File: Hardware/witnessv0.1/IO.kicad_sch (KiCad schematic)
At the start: 3 parts, among them J2 Conn_01x02, J3 Conn_01x08, P1 USB_C_Plug_USB2.0

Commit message: power updates and some esp32 stuff
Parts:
- P1: footprint Connector_USB:USB_C_Receptacle_G-Switch_GT-USB-7010ASV -> KicadLibs:CONN_10164359-00011LF_AMP
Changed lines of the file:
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@@
 			)
 		)
-		(property "Footprint" "Connector_USB:USB_C_Receptacle_G-Switch_GT-USB-7010ASV"
+		(property "Footprint" "KicadLibs:CONN_10164359-00011LF_AMP"
 			(at 234.95 113.03 0)
 			(hide yes)

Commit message: lots of work
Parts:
- added R32: 5.1k, Resistor_SMD:R_0603_1608Metric, symbol Device:R_Small
- added U9: USBLC6-2SC6, Package_TO_SOT_SMD:SOT-23-6, symbol Power_Protection:USBLC6-2SC6
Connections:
- net +BATT: now reaches J2.1 (Pin_1)
- net GND: now reaches J2.2 (Pin_2)
- net GND: now also P1.A1 (GND), P1.A12 (GND), P1.B1 (GND), P1.B12 (GND), R32.1, U9.2 (GND)
- net VBUS: now reaches P1.A4 (VBUS), P1.A9 (VBUS), P1.B4 (VBUS), P1.B9 (VBUS)
- net VBUS: now also U9.5 (VBUS)
- net at P1.A5 (CC): now also R32.2
- net at P1.A6 (D+): now also U9.3 (I/O2)
- net at P1.A7 (D-): now also U9.1 (I/O1)
- new net USB_D+: U9.4 (I/O2), U9.6 (I/O1)
- no-connect marks 0 -> 2
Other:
- note added: "INPUTS"
- note added: "OUTPUTS"
- company: (none) -> WITNESS
- title: (none) -> IO
- moved on the sheet: J2, P1

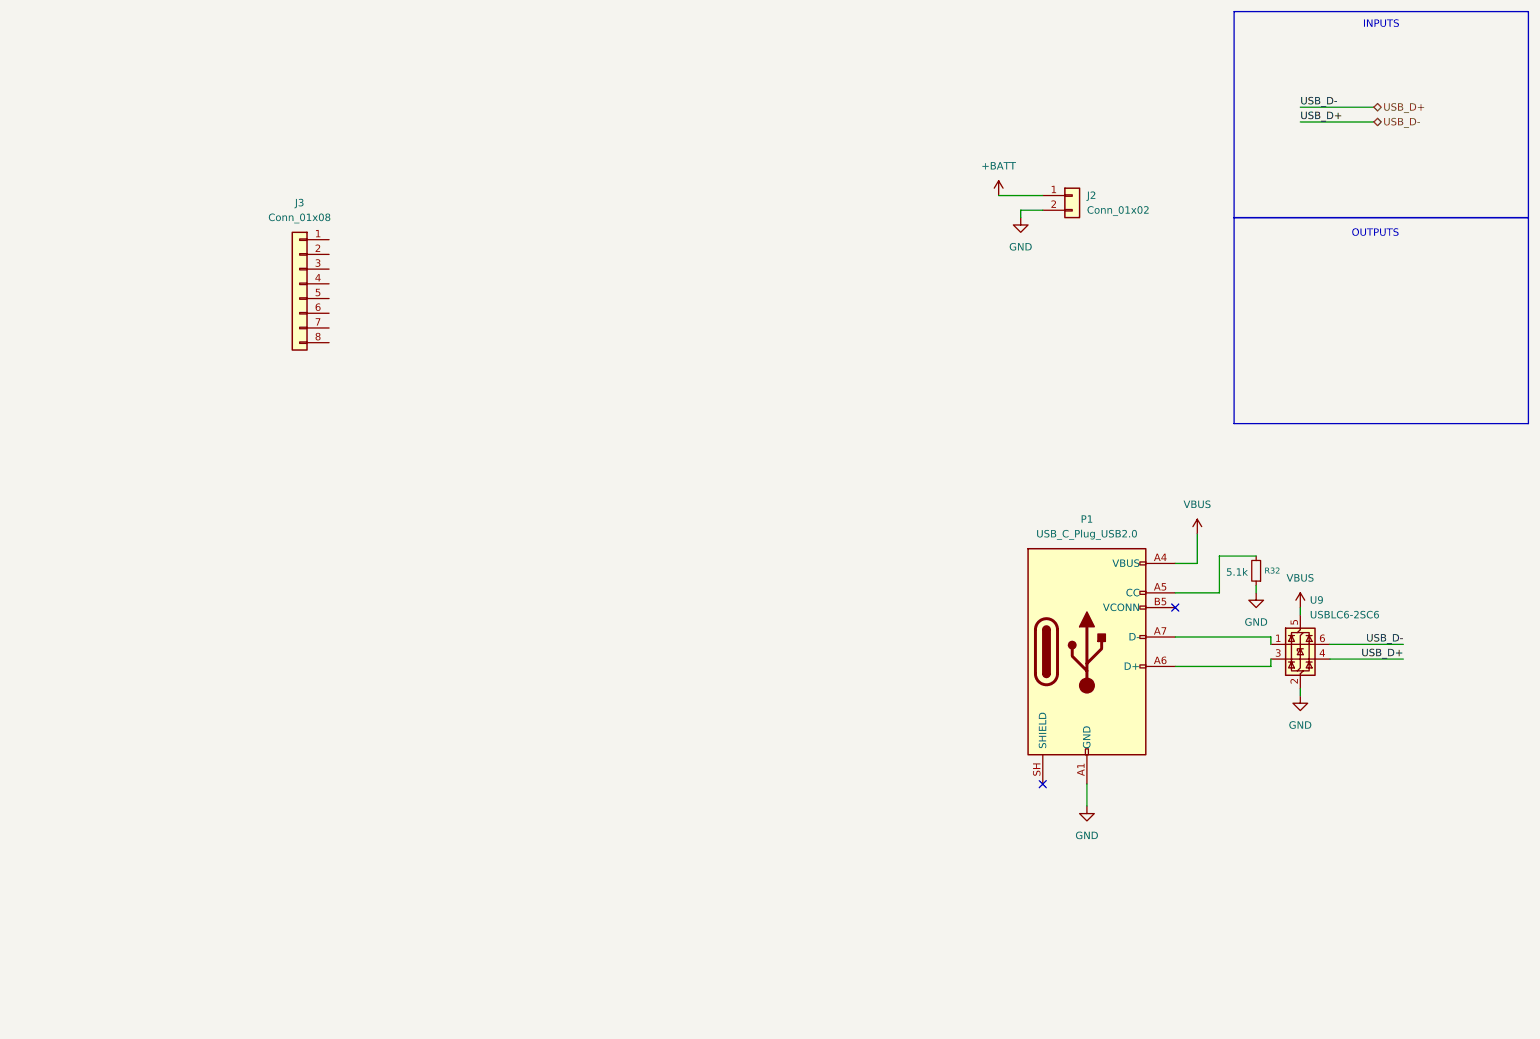
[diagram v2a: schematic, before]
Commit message: micro lock conenctors and sd card soldered to baord and inital palcement done.
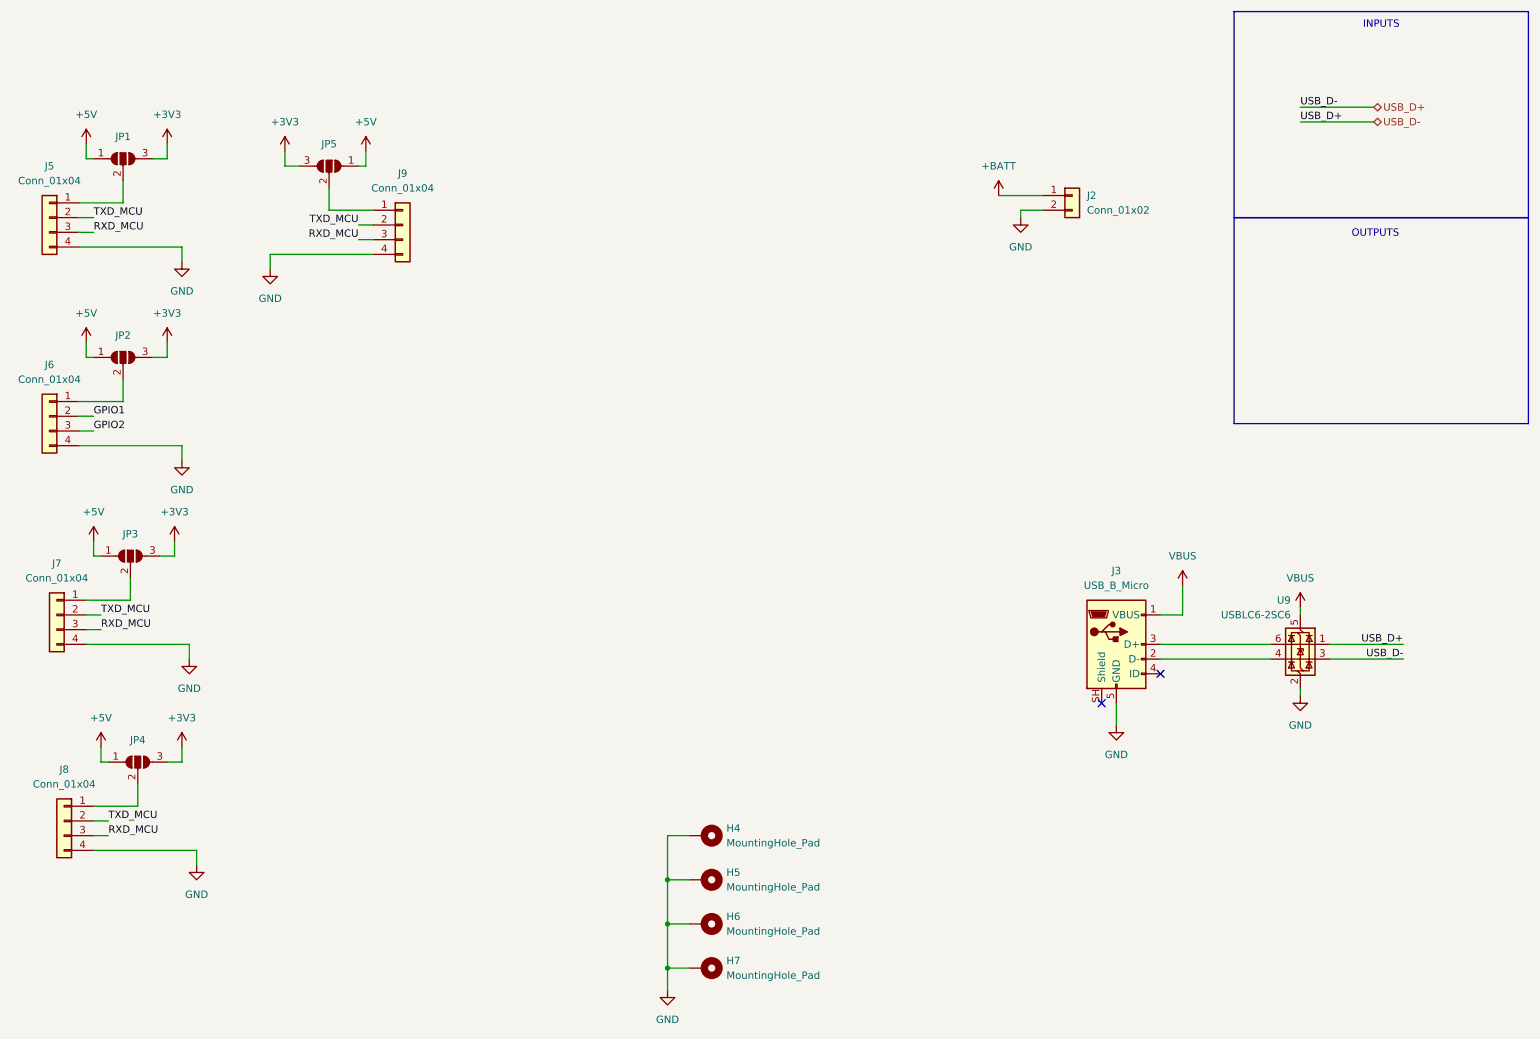
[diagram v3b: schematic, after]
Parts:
- removed J3: Conn_01x08, TerminalBlock_Phoenix:TerminalBlock_Phoenix_MPT-0,5-8-2.54_1x08_P2.54mm_Horizontal, symbol Connector_Generic:Conn_01x08
- removed P1: USB_C_Plug_USB2.0, KicadLibs:CONN_10164359-00011LF_AMP, symbol Connector:USB_C_Plug_USB2.0
- removed R32: 5.1k, Resistor_SMD:R_0603_1608Metric, symbol Device:R_Small
- added H4, H5, H6, H7: MountingHole_Pad, MountingHole:MountingHole_2.2mm_M2_DIN965_Pad, symbol Mechanical:MountingHole_Pad
- added J3: USB_B_Micro, Connector_USB:USB_Micro-B_Amphenol_10118193-0002LF_Horizontal, symbol Connector:USB_B_Micro
- added J5, J6, J7, J8, J9: Conn_01x04, Witness:Molex_MicroLock-2200980471-01x04-Horizontal, symbol Connector_Generic:Conn_01x04
- added JP1, JP2, JP3, JP4, JP5: SolderJumper_3_Open, Jumper:SolderJumper-3_P1.3mm_Open_RoundedPad1.0x1.5mm, symbol Jumper:SolderJumper_3_Open
- J2: footprint Connector_JST:JST_PH_B2B-PH-K_1x02_P2.00mm_Vertical -> Witness:Molex_Micro_Lock_2200980271_01x02_Horizontal
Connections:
- net GND: now also H4.1, H5.1, H6.1, H7.1, J3.5 (GND), J5.4 (Pin_4), J6.4 (Pin_4), J7.4 (Pin_4), J8.4 (Pin_4), J9.4 (Pin_4)
- net USB_D+: now also U9.1 (I/O1), U9.3 (I/O2); no longer U9.4 (I/O2), U9.6 (I/O1)
- net VBUS: now also J3.1 (VBUS)
- new net: J3.2 (D-), U9.4 (I/O2)
- new net: J3.3 (D+), U9.6 (I/O1)
- new net: J8.1 (Pin_1), JP4.2 (C)
- new net: J7.1 (Pin_1), JP3.2 (C)
- new net: J5.1 (Pin_1), JP1.2 (C)
- new net: J9.1 (Pin_1), JP5.2 (C)
- new net: J6.1 (Pin_1), JP2.2 (C)
- new net +3V3: JP1.3 (B), JP2.3 (B), JP3.3 (B), JP4.3 (B), JP5.3 (B)
- new net +5V: JP1.1 (A), JP2.1 (A), JP3.1 (A), JP4.1 (A), JP5.1 (A)
- new net GPIO1: J6.2 (Pin_2)
- new net GPIO2: J6.3 (Pin_3)
- new net RXD_MCU: J5.3 (Pin_3), J7.3 (Pin_3), J8.3 (Pin_3), J9.3 (Pin_3)
- new net TXD_MCU: J5.2 (Pin_2), J7.2 (Pin_2), J8.2 (Pin_2), J9.2 (Pin_2)
